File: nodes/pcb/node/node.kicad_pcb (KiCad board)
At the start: 2 copper layers, 0 parts

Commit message: Rearrange
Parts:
- added BT1: Battery_Cell, Common-Parts-Library:MPD_BK-912-TR, B.Cu at (150.0, 69.5)
- added BT2: Battery_Cell, Common-Parts-Library:MPD_BK-912-TR, B.Cu at (145.8, 143.0)
- added C1: 0.1uF, Capacitor_SMD:C_0603_1608Metric_Pad1.05x0.95mm_HandSolder, F.Cu at (142.4, 127.3)
- added C10: 0.1uF, Capacitor_SMD:C_0603_1608Metric_Pad1.05x0.95mm_HandSolder, B.Cu at (169.1, 82.0)
- added C11: 0.1uF, Capacitor_SMD:C_0603_1608Metric_Pad1.05x0.95mm_HandSolder, B.Cu at (122.0, 138.5)
- added C12: 0.1uF, Capacitor_SMD:C_0603_1608Metric_Pad1.05x0.95mm_HandSolder, B.Cu at (160.3, 140.5)
- added C13: 0.1uF, Capacitor_SMD:C_0603_1608Metric_Pad1.05x0.95mm_HandSolder, F.Cu at (159.1, 136.3)
- added C2: 0.1uF, Capacitor_SMD:C_0603_1608Metric_Pad1.05x0.95mm_HandSolder, F.Cu at (149.8, 143.7)
- added C3: 10uF, Capacitor_Tantalum_SMD:CP_EIA-3216-18_Kemet-A_Pad1.58x1.35mm_HandSolder, F.Cu at (138.2, 133.6)
- added C4: 10uF, Capacitor_Tantalum_SMD:CP_EIA-3216-18_Kemet-A_Pad1.58x1.35mm_HandSolder, F.Cu at (135.6, 141.7)
- added C5: 0.1uF, Capacitor_SMD:C_0603_1608Metric_Pad1.05x0.95mm_HandSolder, F.Cu at (150.3, 140.1)
- added C6: 10uF, Capacitor_Tantalum_SMD:CP_EIA-3216-18_Kemet-A_Pad1.58x1.35mm_HandSolder, F.Cu at (135.9, 141.0)
- added C7: 10uF, Capacitor_Tantalum_SMD:CP_EIA-3216-18_Kemet-A_Pad1.58x1.35mm_HandSolder, F.Cu at (131.8, 136.4)
- added C8: 0.1uF, Capacitor_SMD:C_0603_1608Metric_Pad1.05x0.95mm_HandSolder, F.Cu at (159.2, 134.8)
- added C9: 0.1uF, Capacitor_SMD:C_0603_1608Metric_Pad1.05x0.95mm_HandSolder, B.Cu at (134.5, 68.1)
- added D1: LED_ARGB, LED_SMD:LED_Kingbright_APFA3010_3x1.5mm_Horizontal, B.Cu at (127.8, 70.4)
- added D2: LED_ARGB, LED_SMD:LED_Kingbright_APFA3010_3x1.5mm_Horizontal, B.Cu at (169.4, 76.3)
- added D3: LED_ARGB, LED_SMD:LED_Kingbright_APFA3010_3x1.5mm_Horizontal, B.Cu at (122.6, 140.4)
- added D4: LED_ARGB, LED_SMD:LED_Kingbright_APFA3010_3x1.5mm_Horizontal, B.Cu at (162.2, 141.1)
- added J1: Top Hemisphere, Connector_PinHeader_2.54mm:PinHeader_2x04_P2.54mm_Vertical, F.Cu at (141.1, 81.4)
- added J2: FTDI Basic, Common-Parts-Library:HARWIN_M20-7910642R, F.Cu at (150.2, 74.8)
- added J3: Burner, Connector_PinSocket_2.54mm:PinSocket_1x06_P2.54mm_Vertical, F.Cu at (207.4, 95.2)
- added J4: Port, Connector_PinHeader_2.54mm:PinHeader_1x02_P2.54mm_Vertical, F.Cu at (136.0, 71.1)
- added J5: Port, Connector_PinHeader_2.54mm:PinHeader_1x02_P2.54mm_Vertical, F.Cu at (130.7, 77.1)
- added J6: Bottom Hemisphere, Connector_PinHeader_2.54mm:PinHeader_2x04_P2.54mm_Vertical, F.Cu at (132.7, 129.5)
- added J7: Port, Connector_PinHeader_2.54mm:PinHeader_1x02_P2.54mm_Vertical, F.Cu at (126.5, 126.5)
- added J8: Port, Connector_PinHeader_2.54mm:PinHeader_1x02_P2.54mm_Vertical, F.Cu at (126.9, 135.1)
- added R1: 10k, Resistor_SMD:R_0603_1608Metric_Pad1.05x0.95mm_HandSolder, F.Cu at (162.5, 133.2)
- added R10: 100, Resistor_SMD:R_0603_1608Metric_Pad1.05x0.95mm_HandSolder, B.Cu at (132.3, 72.0)
- added R11: 100, Resistor_SMD:R_0603_1608Metric_Pad1.05x0.95mm_HandSolder, F.Cu at (160.0, 86.2)
- added R12: 100, Resistor_SMD:R_0603_1608Metric_Pad1.05x0.95mm_HandSolder, B.Cu at (114.5, 135.5)
- added R13: 100, Resistor_SMD:R_0603_1608Metric_Pad1.05x0.95mm_HandSolder, B.Cu at (158.6, 139.8)
- added R2: 470, Resistor_SMD:R_0603_1608Metric_Pad1.05x0.95mm_HandSolder, F.Cu at (159.2, 133.2)
- added R3: 470, Resistor_SMD:R_0603_1608Metric_Pad1.05x0.95mm_HandSolder, F.Cu at (156.2, 84.6)
- added R4: 470, Resistor_SMD:R_0603_1608Metric_Pad1.05x0.95mm_HandSolder, F.Cu at (140.1, 73.5)
- added R5: 470, Resistor_SMD:R_0603_1608Metric_Pad1.05x0.95mm_HandSolder, F.Cu at (135.4, 80.9)
- added R6: 470, Resistor_SMD:R_0603_1608Metric_Pad1.05x0.95mm_HandSolder, B.Cu at (140.1, 81.3)
- added R7: 33, Resistor_SMD:R_0603_1608Metric_Pad1.05x0.95mm_HandSolder, B.Cu at (146.2, 81.9)
- added R8: 33, Resistor_SMD:R_0603_1608Metric_Pad1.05x0.95mm_HandSolder, F.Cu at (146.5, 143.7)
- added R9: 33, Resistor_SMD:R_0603_1608Metric_Pad1.05x0.95mm_HandSolder, B.Cu at (153.7, 131.7)
- added U1: MIC5205YM5, Package_TO_SOT_SMD:SOT-23-5, F.Cu at (146.7, 141.2)
- added U2: ATmega328P-AU, Package_QFP:TQFP-32_7x7mm_P0.8mm, F.Cu at (164.5, 77.5)
- added U3: LP2985-3.3, Package_TO_SOT_SMD:SOT-23-5, F.Cu at (152.1, 136.7)
- added U4: ADXL335, Package_CSP:LFCSP-16-1EP_4x4mm_P0.65mm_EP2.1x2.1mm, F.Cu at (142.2, 142.0)
- added U5: WS2811, Package_SO:SSOP-8_3.9x5.05mm_P1.27mm, B.Cu at (133.3, 78.6)
- added U6: WS2811, Package_SO:SSOP-8_3.9x5.05mm_P1.27mm, B.Cu at (156.7, 83.0)
- added U7: WS2811, Package_SO:SSOP-8_3.9x5.05mm_P1.27mm, B.Cu at (116.6, 139.1)
- added U8: WS2811, Package_SO:SSOP-8_3.9x5.05mm_P1.27mm, B.Cu at (162.7, 132.3)
- added Y1: 16MHz, Crystal:Resonator_SMD_muRata_CSTxExxV-3Pin_3.0x1.1mm_HandSoldering, F.Cu at (152.4, 128.9)
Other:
- board outline added: 114.9 x 81.4 mm

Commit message: Tweak
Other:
- board size 114.9 x 81.4 mm -> 164.7 x 81.8 mm
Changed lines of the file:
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@@
-(kicad_pcb (version 20171130) (host pcbnew "(5.0.2)-1")
+(kicad_pcb (version 20171130) (host pcbnew "(5.1.0)-1")
   (general
     (thickness 1.6)
-    (drawings 134)
+    (drawings 190)
     (tracks 0)
     (zones 0)
@@
     (zone_45_only no)
     (trace_min 0.2)
-    (segment_width 0.0254)
-    (edge_width 0.0254)
     (via_size 0.8)
     (via_drill 0.4)
@@
     (uvia_min_size 0.2)
     (uvia_min_drill 0.1)
+    (edge_width 0.0254)
+    (segment_width 0.0254)
     (pcb_text_width 0.3)
     (pcb_text_size 1.5 1.5)
@@
     (solder_mask_min_width 0.25)
     (aux_axis_origin 0 0)
-    (visible_elements 7FFFF7FF)
+    (visible_elements 7FFFFFFF)
     (pcbplotparams
       (layerselection 0x010fc_ffffffff)
@@
     )
   )
+  (gr_line (start 109.80465 64.812001) (end 112.045499 70.881394) (layer Edge.Cuts) (width 0.0254))
+  (gr_line (start 82.47335 64.812) (end 109.80465 64.812001) (layer Edge.Cuts) (width 0.0254))
+  (gr_line (start 80.232501 70.881394) (end 82.47335 64.812) (layer Edge.Cuts) (width 0.0254))
+  (gr_arc (start 79.886148 71.819498) (end 79.117146 72.458744) (angle 150) (layer Edge.Cuts) (width 0.0254))
+  (gr_line (start 74.141816 76.594568) (end 79.117146 72.458744) (layer Edge.Cuts) (width 0.0254))
+  (gr_arc (start 96.139 83.312) (end 73.139 83.312) (angle 17) (layer Edge.Cuts) (width 0.0254))
+  (gr_line (start 119.139 83.312) (end 73.139 83.312) (layer Edge.Cuts) (width 0.000025))
+  (gr_arc (start 96.139 83.312) (end 118.136184 76.594568) (angle 17) (layer Dwgs.User) (width 0.0254))
+  (gr_line (start 113.160854 72.458744) (end 118.136184 76.594568) (layer Edge.Cuts) (width 0.0254))
+  (gr_arc (start 112.391852 71.819498) (end 112.045499 70.881394) (angle 150) (layer Edge.Cuts) (width 0.0254))
+  (gr_line (start 106.68 65.44284) (end 106.68 64.812001) (layer Dwgs.User) (width 0.2))
+  (gr_line (start 107.569 65.44284) (end 106.68 65.44284) (layer Dwgs.User) (width 0.2))
+  (gr_line (start 107.569 67.22084) (end 107.569 65.44284) (layer Dwgs.User) (width 0.2))
+  (gr_line (start 106.68 67.22084) (end 107.569 67.22084) (layer Dwgs.User) (width 0.2))
+  (gr_line (start 106.68 68.74484) (end 106.68 67.22084) (layer Dwgs.User) (width 0.2))
+  (gr_line (start 107.569 68.74484) (end 106.68 68.74484) (layer Dwgs.User) (width 0.2))
+  (gr_line (start 107.569 70.52284) (end 107.569 68.74484) (layer Dwgs.User) (width 0.2))
+  (gr_line (start 106.68 70.52284) (end 107.569 70.52284) (layer Dwgs.User) (width 0.2))
+  (gr_line (start 106.68 72.42784) (end 106.68 70.52284) (layer Dwgs.User) (width 0.2))
+  (gr_line (start 103.758999 75.34884) (end 106.68 72.42784) (layer Dwgs.User) (width 0.2))
+  (gr_line (start 103.399789 75.34884) (end 103.758999 75.34884) (layer Dwgs.User) (width 0.2))
+  (gr_arc (start 96.139 67.95884) (end 103.399789 75.34884) (angle 88.98940468) (layer Dwgs.User) (width 0.2))
+  (gr_line (start 88.519 75.34884) (end 88.878211 75.34884) (layer Dwgs.User) (width 0.2))
+  (gr_line (start 85.598 72.42784) (end 88.519 75.34884) (layer Dwgs.User) (width 0.2))
+  (gr_line (start 85.598 70.52284) (end 85.598 72.42784) (layer Dwgs.User) (width 0.2))
+  (gr_line (start 84.709 70.52284) (end 85.598 70.52284) (layer Dwgs.User) (width 0.2))
+  (gr_line (start 84.709 68.74484) (end 84.709 70.52284) (layer Dwgs.User) (width 0.2))
+  (gr_line (start 85.598 68.74484) (end 84.709 68.74484) (layer Dwgs.User) (width 0.2))
+  (gr_line (start 85.598 67.22084) (end 85.598 68.74484) (layer Dwgs.User) (width 0.2))
+  (gr_line (start 84.709 67.22084) (end 85.598 67.22084) (layer Dwgs.User) (width 0.2))
+  (gr_line (start 84.709 65.44284) (end 84.709 67.22084) (layer Dwgs.User) (width 0.2))
+  (gr_line (start 85.598 65.44284) (end 84.709 65.44284) (layer Dwgs.User) (width 0.2))
+  (gr_line (start 85.598 64.812001) (end 85.598 65.44284) (layer Dwgs.User) (width 0.2))
+  (gr_line (start 74.139 83.312) (end 74.141816 76.594568) (layer Dwgs.User) (width 0.2))
+  (gr_line (start 118.138999 83.312) (end 118.136184 76.594568) (layer Dwgs.User) (width 0.2))
+  (gr_line (start 99.688999 69.112001) (end 99.688999 64.812) (layer Dwgs.User) (width 0.2))
+  (gr_line (start 92.189 69.112001) (end 99.688999 69.112001) (layer Dwgs.User) (width 0.2))
+  (gr_line (start 92.189 64.812001) (end 92.189 69.112001) (layer Dwgs.User) (width 0.2))
+  (gr_line (start 84.139 65.812) (end 82.104145 65.812) (layer Dwgs.User) (width 0.2))
+  (gr_line (start 84.139001 64.812) (end 84.139 65.812) (layer Dwgs.User) (width 0.2))
+  (gr_line (start 108.138999 65.812) (end 110.173855 65.812) (layer Dwgs.User) (width 0.2))
+  (gr_line (start 108.138999 64.812) (end 108.138999 65.812) (layer Dwgs.User) (width 0.2))
+  (gr_arc (start 79.886148 71.819498) (end 79.308835 72.636021) (angle 15.00260496) (layer Dwgs.User) (width 0.2))
+  (gr_line (start 113.257822 73.044283) (end 112.969165 72.636021) (layer Dwgs.User) (width 0.2))
+  (gr_line (start 112.84956 73.332939) (end 113.257822 73.044283) (layer Dwgs.User) (width 0.2))
+  (gr_line (start 111.117621 70.883371) (end 112.84956 73.332939) (layer Dwgs.User) (width 0.2))
+  (gr_line (start 111.525882 70.594714) (end 111.117621 70.883371) (layer Dwgs.User) (width 0.2))
+  (gr_line (start 111.814539 71.002976) (end 111.525882 70.594714) (layer Dwgs.User) (width 0.2))
+  (gr_arc (start 79.886148 71.819498) (end 80.232501 70.881394) (angle 14.99739504) (layer Dwgs.User) (width 0.2))
+  (gr_arc (start 79.886148 71.819498) (end 79.308835 72.636021) (angle 15.00260496) (layer Dwgs.User) (width 0.2))
+  (gr_line (start 79.020178 73.044283) (end 79.308835 72.636021) (layer Dwgs.User) (width 0.2))
+  (gr_line (start 79.42844 73.332939) (end 79.020178 73.044283) (layer Dwgs.User) (width 0.2))
+  (gr_line (start 81.160379 70.883371) (end 79.42844 73.332939) (layer Dwgs.User) (width 0.2))
+  (gr_line (start 80.752118 70.594714) (end 81.160379 70.883371) (layer Dwgs.User) (width 0.2))
+  (gr_line (start 80.463461 71.002976) (end 80.752118 70.594714) (layer Dwgs.User) (width 0.2))
+  (gr_arc (start 79.886148 71.819498) (end 80.232501 70.881394) (angle 14.99739504) (layer Dwgs.User) (width 0.2))
   (gr_line (start 221.057783 89.571896) (end 221.323455 89.35368) (layer Edge.Cuts) (width 0.0254))
   (gr_line (start 225.385415 79.22046) (end 225.385415 78.589621) (layer Edge.Cuts) (width 0.0254))

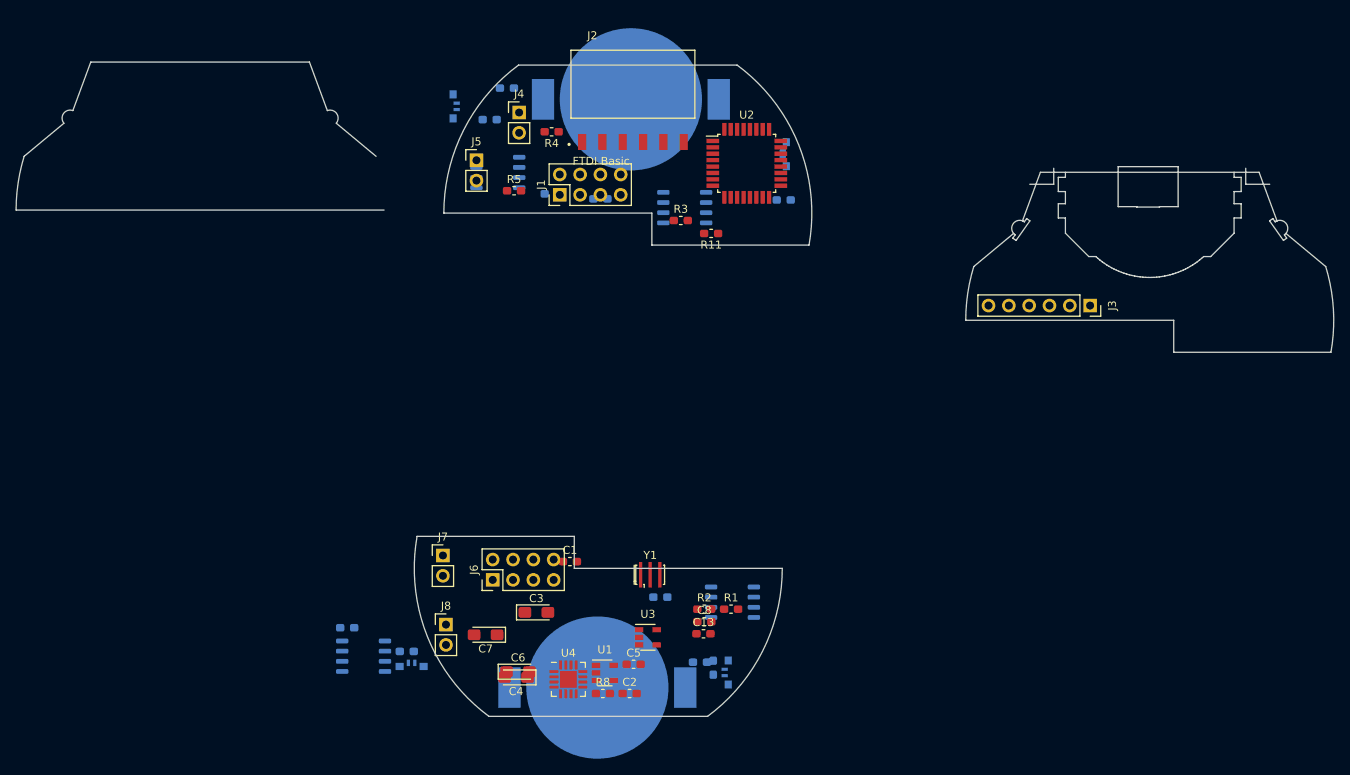
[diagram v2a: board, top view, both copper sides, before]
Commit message: Start simplified Seeed OPL compatible circuit
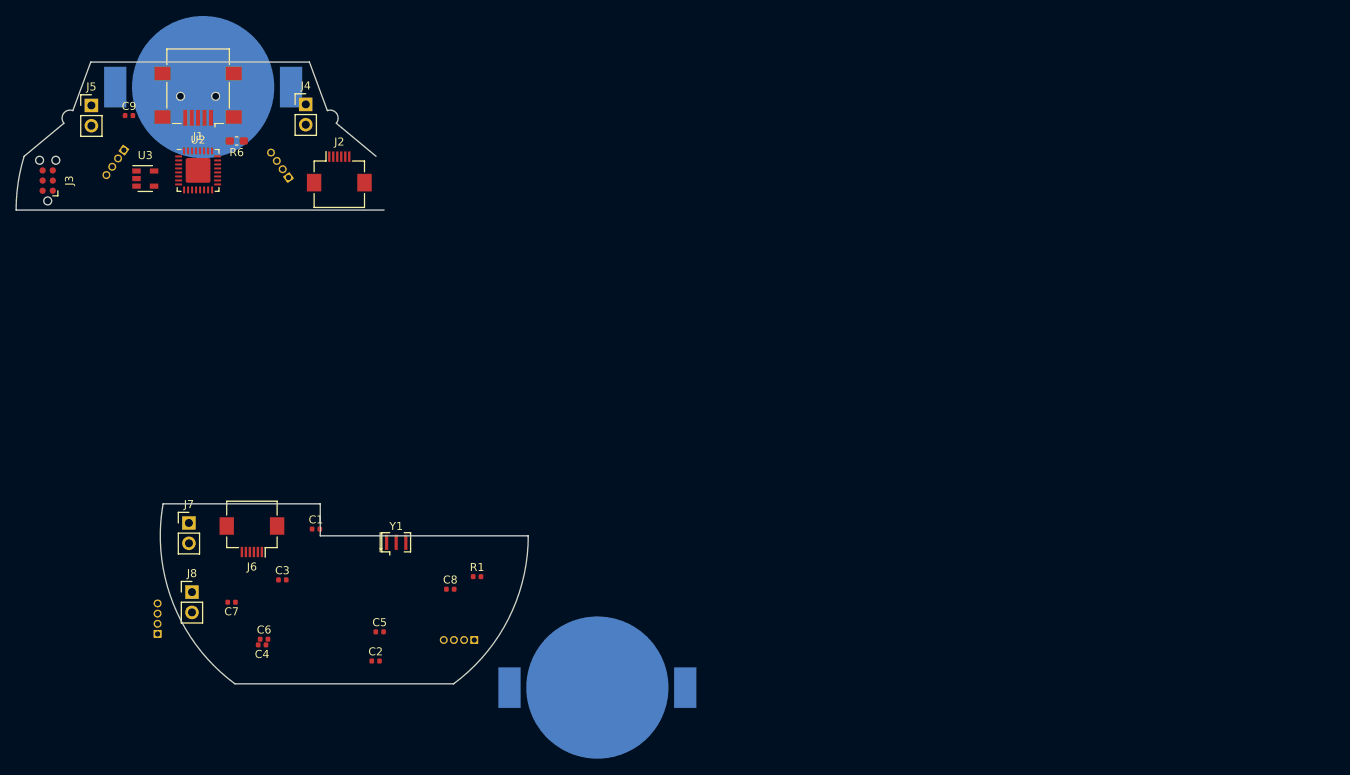
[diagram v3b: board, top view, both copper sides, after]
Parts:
- removed C10, C11, C12, C13: 0.1uF, Capacitor_SMD:C_0603_1608Metric_Pad1.05x0.95mm_HandSolder
- removed R10, R11, R12, R13: 100, Resistor_SMD:R_0603_1608Metric_Pad1.05x0.95mm_HandSolder
- removed R2, R3, R4, R5: 470, Resistor_SMD:R_0603_1608Metric_Pad1.05x0.95mm_HandSolder
- removed R7, R8, R9: 33, Resistor_SMD:R_0603_1608Metric_Pad1.05x0.95mm_HandSolder
- removed U1: MIC5205YM5, Package_TO_SOT_SMD:SOT-23-5
- removed U4: ADXL335, Package_CSP:LFCSP-16-1EP_4x4mm_P0.65mm_EP2.1x2.1mm
- removed U5, U6, U7, U8: WS2811, Package_SO:SSOP-8_3.9x5.05mm_P1.27mm
- C1, C2, C8: footprint Capacitor_SMD:C_0603_1608Metric_Pad1.05x0.95mm_HandSolder -> Capacitor_SMD:C_0402_1005Metric
- C3, C6: value 10uF -> 0.1uF; footprint Capacitor_Tantalum_SMD:CP_EIA-3216-18_Kemet-A_Pad1.58x1.35mm_HandSolder -> Capacitor_SMD:C_0402_1005Metric
- C4: value 10uF -> 1uF; footprint Capacitor_Tantalum_SMD:CP_EIA-3216-18_Kemet-A_Pad1.58x1.35mm_HandSolder -> Capacitor_SMD:C_0402_1005Metric
- C5: value 0.1uF -> 10nF; footprint Capacitor_SMD:C_0603_1608Metric_Pad1.05x0.95mm_HandSolder -> Capacitor_SMD:C_0402_1005Metric
- C7: value 10uF -> 2.2uF; footprint Capacitor_Tantalum_SMD:CP_EIA-3216-18_Kemet-A_Pad1.58x1.35mm_HandSolder -> Capacitor_SMD:C_0402_1005Metric
- C9: footprint Capacitor_SMD:C_0603_1608Metric_Pad1.05x0.95mm_HandSolder -> Capacitor_SMD:C_0402_1005Metric; moved to F.Cu
- D1, D2, D3, D4: value LED_ARGB -> WS2811; footprint LED_SMD:LED_Kingbright_APFA3010_3x1.5mm_Horizontal -> Connector_PinHeader_1.27mm:PinHeader_1x04_P1.27mm_Vertical
- J1: value Top Hemisphere -> Mini-USB; footprint Connector_PinHeader_2.54mm:PinHeader_2x04_P2.54mm_Vertical -> Connector_USB:USB_Mini-B_Lumberg_2486_01_Horizontal
- J2: value FTDI Basic -> TOP-FFC; footprint Common-Parts-Library:HARWIN_M20-7910642R -> Connector_FFC-FPC:Hirose_FH12-6S-0.5SH_1x06-1MP_P0.50mm_Horizontal
- J3: value Burner -> TC2030_NL; footprint Connector_PinSocket_2.54mm:PinSocket_1x06_P2.54mm_Vertical -> Connector:Tag-Connect_TC2030-IDC-NL_2x03_P1.27mm_Vertical
- J6: value Bottom Hemisphere -> BOT-FFC; footprint Connector_PinHeader_2.54mm:PinHeader_2x04_P2.54mm_Vertical -> Connector_FFC-FPC:Hirose_FH12-6S-0.5SH_1x06-1MP_P0.50mm_Horizontal
- R1: footprint Resistor_SMD:R_0603_1608Metric_Pad1.05x0.95mm_HandSolder -> Resistor_SMD:R_0402_1005Metric
- R6: moved to F.Cu
- U2: value ATmega328P-AU -> ATmega328P-MU; footprint Package_QFP:TQFP-32_7x7mm_P0.8mm -> Package_DFN_QFN:VQFN-32-1EP_5x5mm_P0.5mm_EP3.1x3.1mm
- U3: value LP2985-3.3 -> LP2985-5.0
- Y1: footprint Crystal:Resonator_SMD_muRata_CSTxExxV-3Pin_3.0x1.1mm_HandSoldering -> Crystal:Resonator_SMD_muRata_CSTxExxV-3Pin_3.0x1.1mm
- moved J3 131.2 mm to (77.1, 79.6), turned to 90 degrees
- moved U3 85.1 mm to (89.3, 79.4)
- moved D2 82.8 mm to (86.6, 75.8), turned to 145 degrees
- moved U2 68.6 mm to (95.9, 78.4)
- moved BT1 53.5 mm to (96.5, 67.9)
- moved J5 48.6 mm to (82.5, 70.2)
- moved C9 47.4 mm to (87.2, 71.5)
- moved J1 46.9 mm to (95.9, 69.1), turned to 180 degrees
- moved R6 39.9 mm to (100.7, 74.7), turned to 180 degrees
- moved J2 36.9 mm to (113.5, 78.5)
- moved C6 32.0 mm to (104.1, 137.0)
- moved C8 32.0 mm to (127.4, 130.7)
- moved C2 32.0 mm to (118.1, 139.7)
- moved C4 32.0 mm to (103.9, 137.7)
- moved C5 32.0 mm to (118.6, 136.0)
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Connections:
- net Net-(BT2-Pad2) renamed BOT-CELL-MINUS
- BT1 pad 1: Net-(BT1-Pad1) -> TOP-CELL-PLUS
- C1 pad 1: +3V3 -> Net-(C1-Pad1)
- C2 pad 2: Net-(C2-Pad2) -> RST
- C5 pad 1: +5V -> Net-(C5-Pad1)
- C6 pad 1: +3V3 -> +5V
- C9 pad 1: Net-(C9-Pad1) -> +5V
- D1 pad 1: +5V -> Net-(D1-Pad1)
- D1 pad 2: Net-(D1-Pad2) -> GND
- D1 pad 3: Net-(D1-Pad3) -> +5V
- D1 pad 4: Net-(D1-Pad4) -> TOP-LED-DIN
- D2 pad 1: +5V -> TOP-LED-DOUT
- D2 pad 2: Net-(D2-Pad2) -> GND
- D2 pad 3: Net-(D2-Pad3) -> +5V
- D2 pad 4: Net-(D2-Pad4) -> Net-(D1-Pad1)
- D3 pad 1: +5V -> Net-(D3-Pad1)
- D3 pad 2: Net-(D3-Pad2) -> GND
- D3 pad 3: Net-(D3-Pad3) -> +5V
- D3 pad 4: Net-(D3-Pad4) -> BOT-LED-DIN
- D4 pad 1: +5V -> Net-(D4-Pad1)
- D4 pad 2: Net-(D4-Pad2) -> GND
- D4 pad 3: Net-(D4-Pad3) -> +5V
- D4 pad 4: Net-(D4-Pad4) -> Net-(D3-Pad1)
- J1 pad 1: GND -> +5V
- J1 pad 2: Net-(BT1-Pad1) -> RXI
- J1 pad 3: +5V -> TXO
- J1 pad 4: +3V3 -> DTR
- J1 pad 5: Z-ACCEL -> GND
- J1 pad 6: PORT-3 -> (no net)
- J2 pad 1: DTR -> +5V
- J2 pad 2: TXO -> TOP-CELL-PLUS
- J2 pad 3: RXI -> TOP-LED-DOUT
- J2 pad 4: +5V -> PORT-3
- J2 pad 5: GND -> PORT-4
- J3 pad 1: DTR -> +5V
- J3 pad 2: SCK -> MOSI
- J3 pad 4: MOSI -> SCK
- J3 pad 5: +5V -> RST
- J6 pad 1: GND -> +5V
- J6 pad 3: +5V -> BOT-LED-DIN
- J6 pad 4: +3V3 -> BOT-PORT-3
- J6 pad 5: Z-ACCEL -> BOT-PORT-4
- J6 pad 6: PORT-3 -> GND
- J7 pad 2: PORT-3 -> BOT-PORT-3
- J8 pad 2: PORT-4 -> BOT-PORT-4
- R1 pad 2: Net-(C2-Pad2) -> RST
- R6 pad 1: /NeoPixel 1/DIN -> TOP-LED-DIN
- U2 pad 1: Net-(R5-Pad2) -> PORT-2
- U2 pad 12: Net-(R2-Pad2) -> PORT-3
- U2 pad 13: Net-(R3-Pad2) -> PORT-4
- U2 pad 20: +3V3 -> Net-(C1-Pad1)
- U2 pad 29: Net-(C2-Pad2) -> RST
- U2 pad 32: Net-(R4-Pad2) -> PORT-1
- U3 pad 1: +5V -> +BATT
- U3 pad 3: +5V -> +BATT
- U3 pad 4: Net-(U3-Pad4) -> Net-(C5-Pad1)
- U3 pad 5: +3V3 -> +5V
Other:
- board size 164.7 x 81.8 mm -> 64 x 77.7 mm
